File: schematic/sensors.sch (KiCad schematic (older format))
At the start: 41 parts, among them J11 Conn_01x02, J12 Conn_01x02, J13 Conn_01x02, J14 Conn_01x02, J15 Conn_01x02, J16 Conn_01x02, J17 Conn_01x04, SW2 SW_DIP_x03

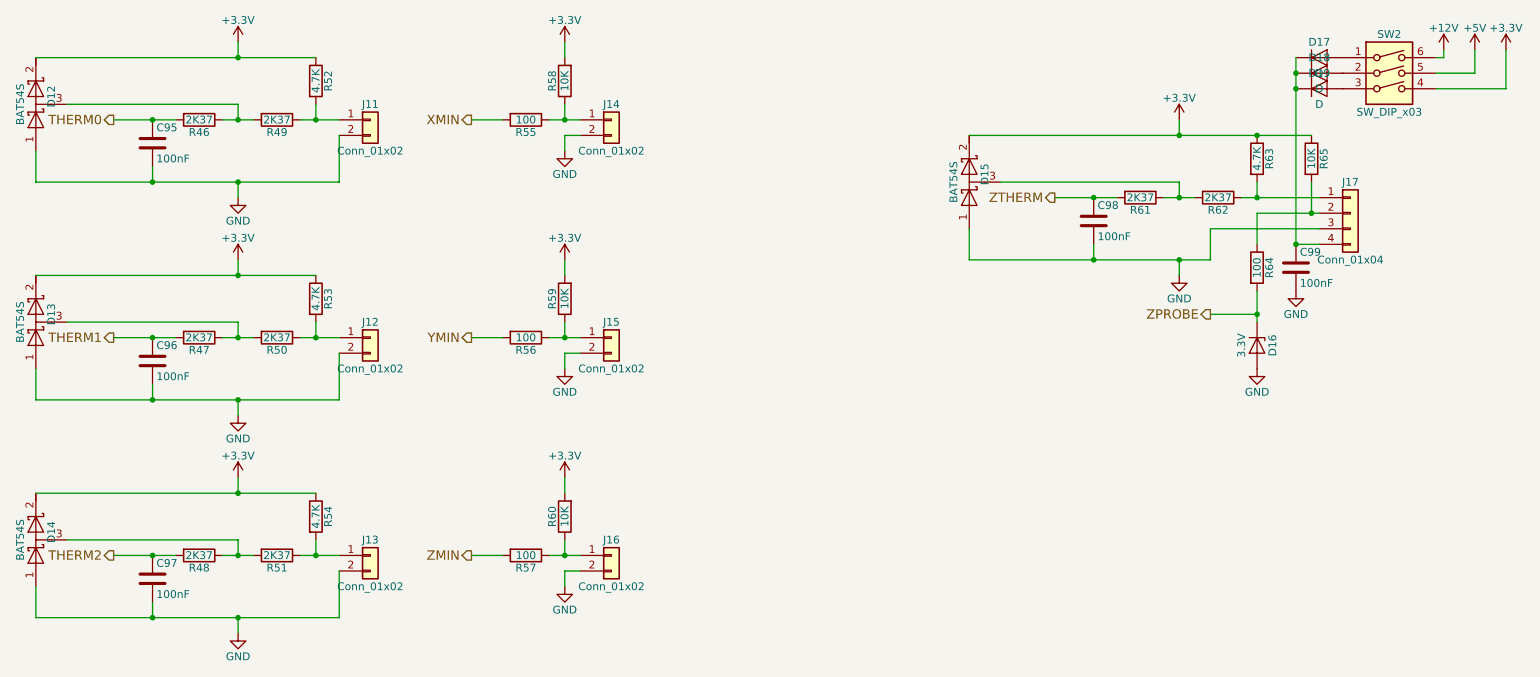
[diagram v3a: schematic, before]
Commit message: Changed footprint size of some capacitors
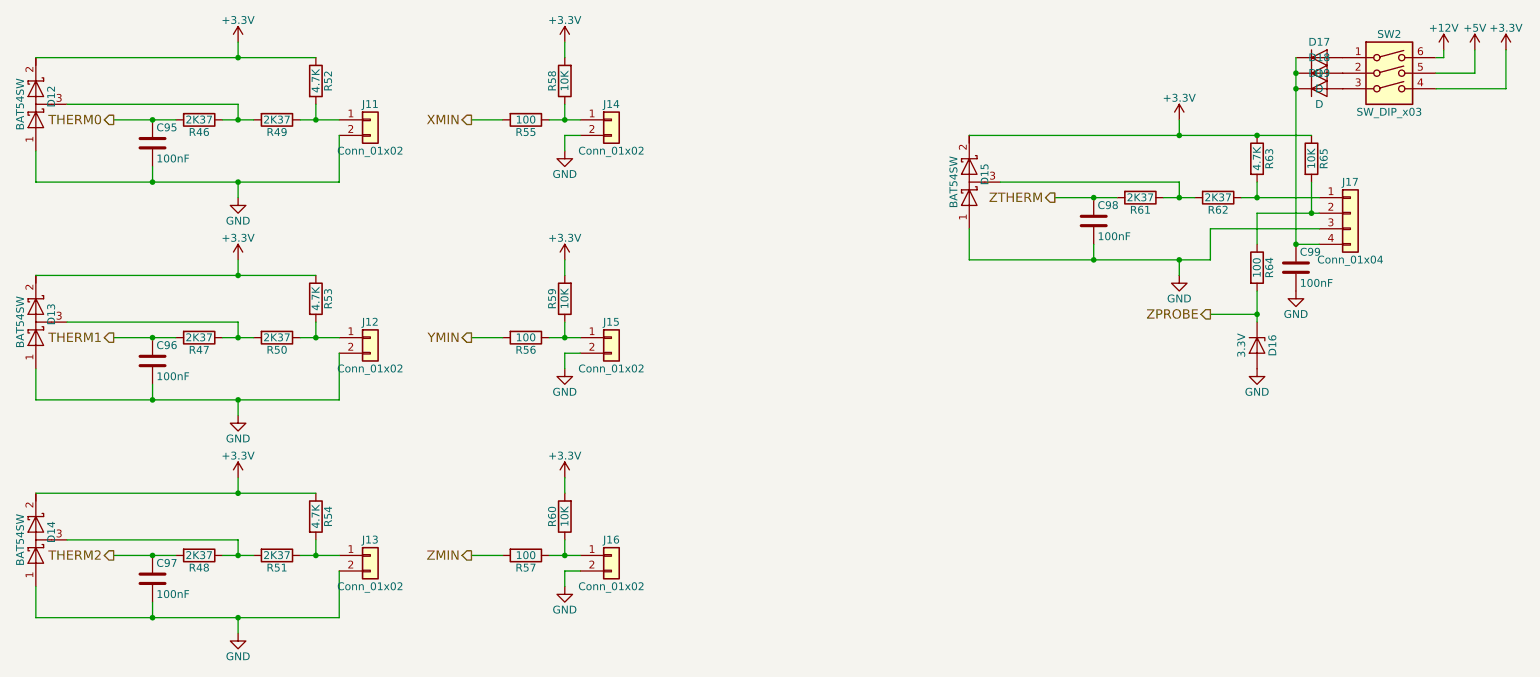
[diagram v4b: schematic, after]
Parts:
- D12, D13, D14, D15: value BAT54S -> BAT54SW
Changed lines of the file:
@@
 P 6900 1750
 F 0 "D15" H 6950 1650 50  0000 C CNN
-F 1 "BAT54S" H 6900 1850 50  0000 C CNN
+F 1 "BAT54SW" H 6900 1850 50  0000 C CNN
 F 2 "TO_SOT_Packages_SMD:SOT-23" H 6900 1750 50  0001 C CNN
 F 3 "" H 6900 1750 50  0001 C CNN
@@
 P 900 2650
 F 0 "D13" H 950 2550 50  0000 C CNN
-F 1 "BAT54S" H 900 2750 50  0000 C CNN
+F 1 "BAT54SW" H 900 2750 50  0000 C CNN
 F 2 "TO_SOT_Packages_SMD:SOT-23" H 900 2650 50  0001 C CNN
 F 3 "" H 900 2650 50  0001 C CNN
@@
 P 900 4050
 F 0 "D14" H 950 3950 50  0000 C CNN
-F 1 "BAT54S" H 900 4150 50  0000 C CNN
+F 1 "BAT54SW" H 900 4150 50  0000 C CNN
 F 2 "TO_SOT_Packages_SMD:SOT-23" H 900 4050 50  0001 C CNN
 F 3 "" H 900 4050 50  0001 C CNN
@@
 P 900 1250
 F 0 "D12" H 950 1150 50  0000 C CNN
-F 1 "BAT54S" H 900 1350 50  0000 C CNN
+F 1 "BAT54SW" H 900 1350 50  0000 C CNN
 F 2 "TO_SOT_Packages_SMD:SOT-23" H 900 1250 50  0001 C CNN
 F 3 "" H 900 1250 50  0001 C CNN

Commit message: updated footprint bat54sw
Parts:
- D12, D13, D14, D15: footprint TO_SOT_Packages_SMD:SOT-23 -> TO_SOT_Packages_SMD:SOT-323_SC-70
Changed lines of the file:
@@
 F 0 "D15" H 6950 1650 50  0000 C CNN
 F 1 "BAT54SW" H 6900 1850 50  0000 C CNN
-F 2 "TO_SOT_Packages_SMD:SOT-23" H 6900 1750 50  0001 C CNN
+F 2 "TO_SOT_Packages_SMD:SOT-323_SC-70" H 6900 1750 50  0001 C CNN
 F 3 "" H 6900 1750 50  0001 C CNN
 	1    6900 1750
@@
 F 0 "D13" H 950 2550 50  0000 C CNN
 F 1 "BAT54SW" H 900 2750 50  0000 C CNN
-F 2 "TO_SOT_Packages_SMD:SOT-23" H 900 2650 50  0001 C CNN
+F 2 "TO_SOT_Packages_SMD:SOT-323_SC-70" H 900 2650 50  0001 C CNN
 F 3 "" H 900 2650 50  0001 C CNN
 	1    900  2650
@@
 F 0 "D14" H 950 3950 50  0000 C CNN
 F 1 "BAT54SW" H 900 4150 50  0000 C CNN
-F 2 "TO_SOT_Packages_SMD:SOT-23" H 900 4050 50  0001 C CNN
+F 2 "TO_SOT_Packages_SMD:SOT-323_SC-70" H 900 4050 50  0001 C CNN
 F 3 "" H 900 4050 50  0001 C CNN
 	1    900  4050
@@
 F 0 "D12" H 950 1150 50  0000 C CNN
 F 1 "BAT54SW" H 900 1350 50  0000 C CNN
-F 2 "TO_SOT_Packages_SMD:SOT-23" H 900 1250 50  0001 C CNN
+F 2 "TO_SOT_Packages_SMD:SOT-323_SC-70" H 900 1250 50  0001 C CNN
 F 3 "" H 900 1250 50  0001 C CNN
 	1    900  1250
